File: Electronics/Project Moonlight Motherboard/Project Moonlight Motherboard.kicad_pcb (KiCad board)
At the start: 2 copper layers, 104.9 x 57.5 mm, 33 parts, among them M1 AO3400A, M2 AO3400A, M3 AO3400A, U1 Pico, U2 TMC2209_SILENTSTEPSTICK, U3 TMC2209_SILENTSTEPSTICK, U4 TMC2209_SILENTSTEPSTICK, U5 TMC2209_SILENTSTEPSTICK

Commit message: added headers for screen and rotary encoder, more tweaks
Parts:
- added ABL1: B2B-XH-A, B2B-XH-A:JST_B2B-XH-A, F.Cu at (193.1, 73.3)
- added R4: RC1206JR-134K7L, RC1206JR-134K7L:RESC3216X65, F.Cu at (202.8, 71.5)
- added R5: RC1206JR-134K7L, RC1206JR-134K7L:RESC3216X65, F.Cu at (202.8, 74.8)
- added R6: RC1206JR-134K7L, RC1206JR-134K7L:RESC3216X65, F.Cu at (201.5, 96.5)
- added REN1: PEC11H-4015F-S0016, Connector_PinHeader_2.54mm:PinHeader_1x04_P2.54mm_Vertical, F.Cu at (195.8, 108.1)
- added SCRN1: SSD1306, Connector_PinHeader_2.54mm:PinHeader_1x04_P2.54mm_Vertical, F.Cu at (195.8, 111.7)
- added ZES1: B2B-XH-A, B2B-XH-A:JST_B2B-XH-A, F.Cu at (184.2, 73.3)
- moved THM3 0.10 mm to (175.4, 73.3)
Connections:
- C5 pad 1: Net-(C5-Pad1) -> Net-(U1-GPIO13)
- C6 pad 1: Net-(C6-Pad1) -> Net-(U1-GPIO12)
- C7 pad 1: Net-(C7-Pad1) -> Net-(U1-GPIO11)
- R1 pad 2: Net-(C5-Pad1) -> Net-(U1-GPIO13)
- R2 pad 2: Net-(C6-Pad1) -> Net-(U1-GPIO12)
- R3 pad 2: Net-(C7-Pad1) -> Net-(U1-GPIO11)
- THM1 pad 2: Net-(C5-Pad1) -> Net-(U1-GPIO13)
- THM2 pad 2: Net-(C6-Pad1) -> Net-(U1-GPIO12)
- THM3 pad 2: Net-(C7-Pad1) -> Net-(U1-GPIO11)
- U1 pad 1: unconnected-(U1-GPIO0-Pad1) -> Net-(U1-GPIO0)
- U1 pad 14: unconnected-(U1-GPIO10-Pad14) -> Net-(REN1-W)
- U1 pad 15: unconnected-(U1-GPIO11-Pad15) -> Net-(U1-GPIO11)
- U1 pad 16: unconnected-(U1-GPIO12-Pad16) -> Net-(U1-GPIO12)
- U1 pad 17: unconnected-(U1-GPIO13-Pad17) -> Net-(U1-GPIO13)
- U1 pad 19: unconnected-(U1-GPIO14-Pad19) -> Net-(REN1-B)
- U1 pad 2: unconnected-(U1-GPIO1-Pad2) -> Net-(U1-GPIO1)
- U1 pad 20: unconnected-(U1-GPIO15-Pad20) -> Net-(REN1-A)
- U1 pad 31: unconnected-(U1-GPIO26_ADC0-Pad31) -> Net-(SCRN1-SDA)
- U1 pad 32: unconnected-(U1-GPIO27_ADC1-Pad32) -> Net-(SCRN1-SCL)
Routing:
- net +3V3: track 131.5 -> 205.0 mm, vias 4 -> 7
- net Net-(U1-GPIO12): track 0.00 -> 64.1 mm, vias 0 -> 3
- net Net-(REN1-A): track 0.00 -> 63.8 mm, vias 0 -> 6
- net Net-(REN1-B): track 0.00 -> 62.2 mm, vias 0 -> 6
- net Net-(REN1-W): track 0.00 -> 56.5 mm, vias 0 -> 5
- net Net-(C6-Pad1): track 49.6 -> 0.00 mm, vias 3 -> 0
- net Net-(U1-GPIO13): track 0.00 -> 45.0 mm, vias 0 -> 1
- net Net-(U1-GPIO11): track 0.00 -> 34.7 mm, vias 0 -> 1
- net Net-(C5-Pad1): track 33.5 -> 0.00 mm, vias 1 -> 0
- net Net-(U1-GPIO0): track 0.00 -> 32.0 mm, vias 0 -> 1
- net Net-(SCRN1-SDA): track 0.00 -> 29.7 mm, vias 0 -> 2
- net GNDREF: track 412.5 -> 439.4 mm, vias 4 -> 5
- net Net-(SCRN1-SCL): track 0.00 -> 24.7 mm, vias 0 -> 2
- net Net-(C7-Pad1): track 23.8 -> 0.00 mm, vias 1 -> 0
- net Net-(U1-GPIO1): track 0.00 -> 19.3 mm, vias 0 -> 1
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
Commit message: added a random resistor for UART - coming soon...
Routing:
- net Net-(U1-GPIO17): track 103.0 -> 105.4 mm
- net Net-(U1-GPIO9): track 79.9 -> 78.4 mm
- net Net-(U1-GPIO5): track 92.7 -> 91.8 mm
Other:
- outline, holes or cut-outs redrawn

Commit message: fixed schematic & added 3d model for MCU
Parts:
- removed ZES1: B2B-XH-A, B2B-XH-A:JST_B2B-XH-A
- added R7: RC0603FR-131KL, RC0603FR-131KL:0603, F.Cu at (51.2, 106.3)
- added Z_END1: B2B-XH-A, B2B-XH-A:JST_B2B-XH-A, F.Cu at (51.2, 87.0)
- U1: value Pico -> STM32F407IEHx; footprint MCU_RaspberryPi_and_Boards:RPi_Pico_SMD_TH -> Package_BGA:UFBGA-201_10x10mm_Layout15x15_P0.65mm
- moved C4 158.6 mm to (28.5, 111.3), turned to 0 degrees
- moved REN1 156.4 mm to (39.4, 107.6), turned to 0 degrees
- moved SCRN1 151.8 mm to (44.1, 107.6), turned to 0 degrees
- moved ABL1 151.6 mm to (41.6, 72.4), turned to 0 degrees
- moved C3 147.1 mm to (28.5, 99.1), turned to 0 degrees
- moved C2 136.8 mm to (28.5, 87.0), turned to 0 degrees
- moved R4 129.2 mm to (73.9, 80.4)
- moved R5 129.2 mm to (73.9, 83.7)
- moved R6 127.9 mm to (73.9, 87.0), turned to 0 degrees
- moved C1 127.9 mm to (28.5, 74.8), turned to 0 degrees
- moved C7 126.5 mm to (47.9, 110.6), turned to 0 degrees
- moved THM3 124.4 mm to (51.2, 79.7), turned to 0 degrees
- moved C6 122.8 mm to (47.9, 108.5), turned to 0 degrees
- moved PWR1 120.5 mm to (80.0, 95.0)
- moved C5 119.3 mm to (47.9, 106.3), turned to 0 degrees
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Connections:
- ABL1 pad 1: Net-(U1-GPIO1) -> ABL
- C5 pad 1: Net-(U1-GPIO13) -> T2
- C6 pad 1: Net-(U1-GPIO12) -> T1
- C7 pad 1: Net-(U1-GPIO11) -> T0
- M1 pad 1: Net-(U1-GPIO20) -> FAN1
- M2 pad 1: Net-(U1-GPIO21) -> FAN2
- M3 pad 1: Net-(U1-GPIO22) -> FAN3
- MOTOR_Y1 pad 1: Net-(U3-M1B) -> Net-(U4-M1B)
- MOTOR_Y1 pad 2: Net-(U3-M1A) -> Net-(U4-M1A)
- MOTOR_Y1 pad 3: Net-(U3-M2A) -> Net-(U4-M2A)
- MOTOR_Y1 pad 4: Net-(U3-M2B) -> Net-(U4-M2B)
- MOTOR_Z1 pad 1: Net-(U4-M1B) -> Net-(U3-M1B)
- MOTOR_Z1 pad 2: Net-(U4-M1A) -> Net-(U3-M1A)
- MOTOR_Z1 pad 3: Net-(U4-M2A) -> Net-(U3-M2A)
- MOTOR_Z1 pad 4: Net-(U4-M2B) -> Net-(U3-M2B)
- PWR1 pad 1: VCC -> Net-(F1-Pad1)
- Q1 pad 4: Net-(Q1-G) -> HOTEND
- Q2 pad 4: Net-(Q2-G) -> BED
- R1 pad 2: Net-(U1-GPIO13) -> T2
- R2 pad 2: Net-(U1-GPIO12) -> T1
- R3 pad 2: Net-(U1-GPIO11) -> T0
- R4 pad 1: Net-(U1-GPIO0) -> Z_END
- R5 pad 1: Net-(U1-GPIO1) -> ABL
- R6 pad 1: Net-(REN1-W) -> EN_BTN
- REN1 pad 1: Net-(REN1-A) -> EN_FOR
- REN1 pad 2: Net-(REN1-B) -> EN_REV
- REN1 pad 4: Net-(REN1-W) -> EN_BTN
- SCRN1 pad 3: Net-(SCRN1-SCL) -> SCRN_SCL
- SCRN1 pad 4: Net-(SCRN1-SDA) -> SCRN_SDA
- THM1 pad 2: Net-(U1-GPIO13) -> T2
- THM2 pad 2: Net-(U1-GPIO12) -> T1
- THM3 pad 2: Net-(U1-GPIO11) -> T0
- U2 pad 10: Net-(U1-GPIO2) -> STEP_M1
- U2 pad 12: unconnected-(U2-UART-Pad12) -> UART_RX
- U2 pad 16: Net-(U1-GPIO17) -> EN_M1
- U2 pad 18: unconnected-(U2-DIAG-Pad18) -> DIAG_M1
- U2 pad 9: Net-(U1-GPIO6) -> DIR_M1
- U3 pad 10: Net-(U1-GPIO3) -> STEP_M2
- U3 pad 12: unconnected-(U3-UART-Pad12) -> UART_RX
- U3 pad 16: Net-(U1-GPIO17) -> EN_M2
- U3 pad 18: unconnected-(U3-DIAG-Pad18) -> DIAG_M2
- U3 pad 9: Net-(U1-GPIO7) -> DIR_M2
- U4 pad 10: Net-(U1-GPIO4) -> STEP_M3
- U4 pad 12: unconnected-(U4-UART-Pad12) -> UART_RX
- U4 pad 16: Net-(U1-GPIO16) -> EN_M3
- U4 pad 18: unconnected-(U4-DIAG-Pad18) -> DIAG_M3
- U4 pad 9: Net-(U1-GPIO8) -> DIR_M3
- U5 pad 10: Net-(U1-GPIO5) -> STEP_M4
- U5 pad 12: unconnected-(U5-UART-Pad12) -> UART_RX
- U5 pad 16: Net-(U1-GPIO16) -> EN_M4
- U5 pad 18: unconnected-(U5-DIAG-Pad18) -> DIAG_M4
- U5 pad 9: Net-(U1-GPIO9) -> DIR_M4
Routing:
- net GNDREF: track 439.4 -> 0.00 mm, vias 5 -> 0
- net +3V3: track 205.0 -> 0.00 mm, vias 7 -> 0
- net VCC: track 201.0 -> 0.00 mm, vias 4 -> 0
- net Net-(U1-GPIO2): track 106.3 -> 0.00 mm
- net Net-(U1-GPIO17): track 105.4 -> 0.00 mm, vias 4 -> 0
- net Net-(U1-GPIO6): track 100.8 -> 0.00 mm
- net Net-(U1-GPIO16): track 97.0 -> 0.00 mm, vias 5 -> 0
- net Net-(U1-GPIO5): track 91.8 -> 0.00 mm, vias 1 -> 0
- net Net-(U1-GPIO9): track 78.4 -> 0.00 mm
- net Net-(U1-GPIO4): track 78.1 -> 0.00 mm, vias 1 -> 0
- net Net-(U1-GPIO3): track 72.4 -> 0.00 mm, vias 1 -> 0
- net Net-(U1-GPIO8): track 72.3 -> 0.00 mm, vias 2 -> 0
- net Net-(U1-GPIO12): track 64.1 -> 0.00 mm, vias 3 -> 0
- net Net-(REN1-A): track 63.8 -> 0.00 mm, vias 6 -> 0
- net Net-(REN1-B): track 62.2 -> 0.00 mm, vias 6 -> 0
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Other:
- board size 104.9 x 57.5 mm -> 105 x 50 mm

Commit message: slowly updating lmao
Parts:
- removed U1: STM32F407IEHx, Package_BGA:UFBGA-201_10x10mm_Layout15x15_P0.65mm
- added U6: STM32H563VITx, Package_QFP:LQFP-100_14x14mm_P0.5mm, F.Cu at (176.6, 95.7)
- moved SCRN1 157.4 mm to (200.6, 91.0)
- moved REN1 156.7 mm to (195.2, 91.0)
- moved PWR1 121.8 mm to (201.0, 108.6)
- moved U2 119.3 mm to (135.7, 117.9), turned to -90 degrees
- moved BED1 114.5 mm to (180.8, 127.7)
- moved M1 113.0 mm to (183.7, 75.5), turned to 90 degrees
- moved M2 109.8 mm to (179.1, 75.5), turned to 90 degrees
- moved M3 106.8 mm to (174.4, 75.5), turned to 90 degrees
- moved Q2 103.1 mm to (184.7, 114.1), turned to -90 degrees
- moved HOTEND1 100.8 mm to (169.9, 127.7)
- moved Q1 92.8 mm to (173.8, 114.1), turned to -90 degrees
- moved U3 87.2 mm to (113.1, 117.9), turned to -90 degrees
- moved MOTOR_X1 77.0 mm to (135.7, 106.0)
- moved MOTOR_Y1 72.8 mm to (135.7, 94.1), turned to 180 degrees
- moved U4 72.7 mm to (135.7, 82.1), turned to 90 degrees
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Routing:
- net GNDREF: track 0.00 -> 30.5 mm
- net HOTEND: track 0.00 -> 28.2 mm
- net BED: track 0.00 -> 19.7 mm
- net Net-(BED1-Pad01): track 0.00 -> 11.3 mm
- net Net-(HOTEND1-Pad01): track 0.00 -> 11.1 mm
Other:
- board size 105 x 50 mm -> 105 x 56 mm

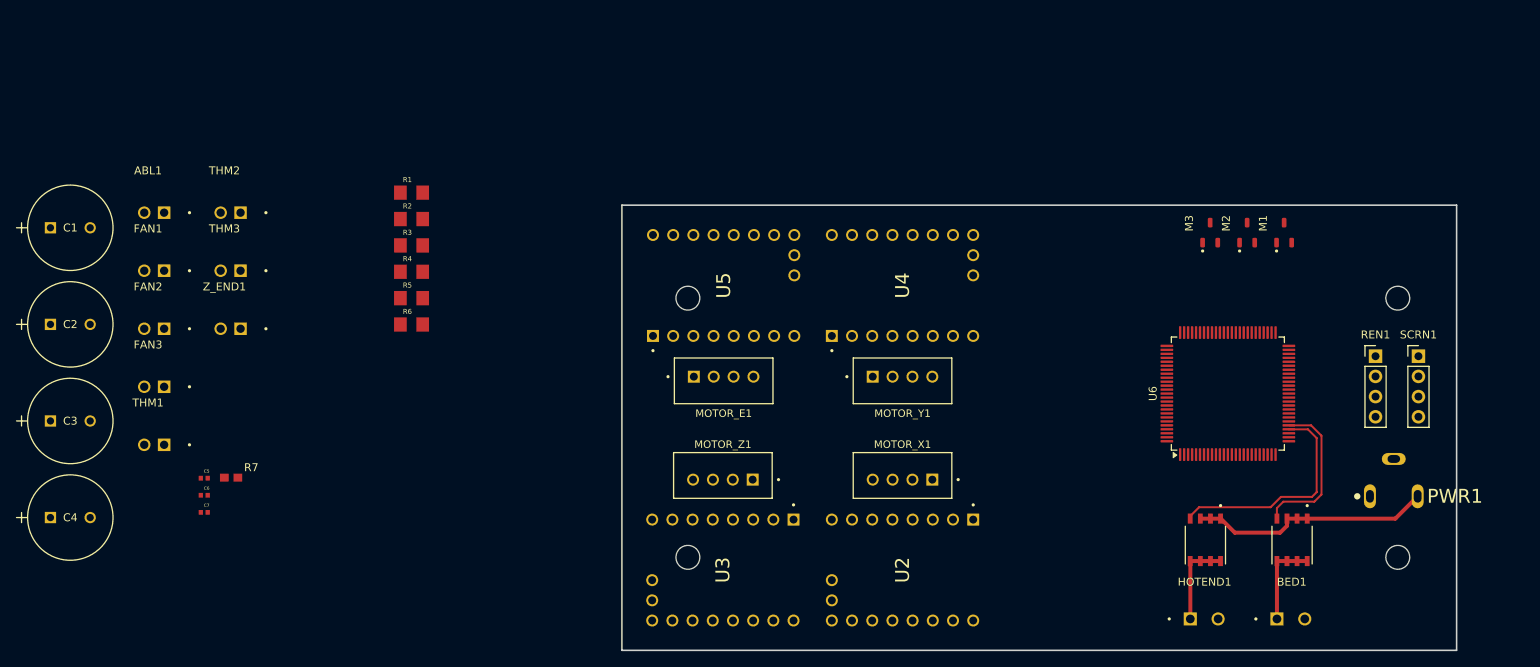
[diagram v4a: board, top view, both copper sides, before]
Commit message: added more parts and more routing done
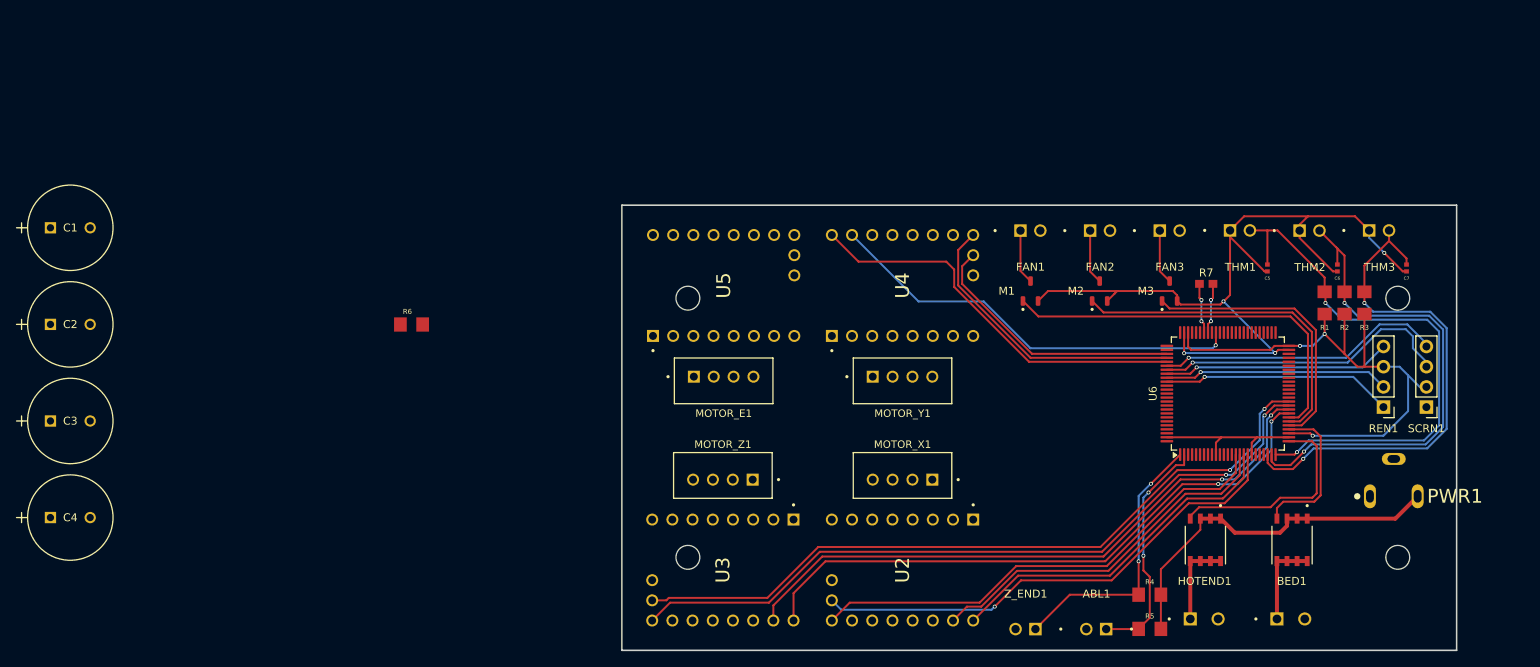
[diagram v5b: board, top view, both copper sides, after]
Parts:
- moved C7 154.3 mm to (199.1, 79.9), turned to -90 degrees
- moved C6 145.4 mm to (190.4, 79.9), turned to -90 degrees
- moved THM3 144.5 mm to (195.7, 75.7), turned to 180 degrees
- moved THM1 139.0 mm to (178.2, 75.7), turned to 180 degrees
- moved C5 136.3 mm to (181.6, 79.9), turned to -90 degrees
- moved THM2 135.8 mm to (186.9, 75.7), turned to 180 degrees
- moved ABL1 129.6 mm to (160.1, 124.8)
- moved FAN3 129.1 mm to (169.3, 75.7), turned to 180 degrees
- moved R7 125.1 mm to (173.9, 81.9), turned to 180 degrees
- moved R3 120.1 mm to (193.8, 84.3), turned to 90 degrees
- moved FAN2 119.5 mm to (160.6, 75.7), turned to 180 degrees
- moved R2 117.8 mm to (191.3, 84.3), turned to 90 degrees
- moved R1 115.7 mm to (188.8, 84.3), turned to 90 degrees
- moved FAN1 110.3 mm to (151.8, 75.7), turned to 180 degrees
- moved Z_END1 106.9 mm to (151.2, 124.8)
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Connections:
- U6 pad 1: unconnected-(U6-PE2-Pad1) -> Z_END
- U6 pad 2: unconnected-(U6-PE3-Pad2) -> ABL
- U6 pad 26: unconnected-(U6-PA3-Pad26) -> HOTEND
- U6 pad 29: HOTEND -> BED
- U6 pad 30: BED -> FAN3
- U6 pad 31: FAN1 -> FAN2
- U6 pad 32: FAN2 -> FAN1
- U6 pad 33: EN_M2 -> STEP_M2
- U6 pad 34: STEP_M2 -> EN_M2
- U6 pad 36: unconnected-(U6-PB1-Pad36) -> DIAG_M2
- U6 pad 64: DIAG_M2 -> unconnected-(U6-PC7-Pad64)
- U6 pad 65: EN_M3 -> EN_M4
- U6 pad 67: FAN3 -> unconnected-(U6-PA8-Pad67)
- U6 pad 68: unconnected-(U6-PA9-Pad68) -> UART_TX
- U6 pad 69: ABL -> UART_RX
- U6 pad 70: Z_END -> unconnected-(U6-PA11-Pad70)
- U6 pad 78: DIR_M3 -> DIAG_M3
- U6 pad 79: DIAG_M3 -> EN_M3
- U6 pad 80: EN_M4 -> DIR_M3
- U6 pad 83: EN_FOR -> EN_BTN
- U6 pad 85: EN_BTN -> EN_FOR
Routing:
- net GNDREF: track 30.5 -> 171.3 mm, vias 0 -> 4
- net EN_M2: track 0.00 -> 93.3 mm, vias 0 -> 2
- net DIAG_M2: track 0.00 -> 92.4 mm, vias 0 -> 2
- net STEP_M2: track 0.00 -> 79.0 mm, vias 0 -> 2
- net DIR_M2: track 0.00 -> 77.2 mm, vias 0 -> 2
- net +3V3: track 0.00 -> 70.5 mm, vias 0 -> 3
- net T2: track 0.00 -> 69.1 mm, vias 0 -> 2
- net T0: track 0.00 -> 64.6 mm, vias 0 -> 2
- net T1: track 0.00 -> 63.1 mm, vias 0 -> 2
- net DIAG_M1: track 0.00 -> 62.8 mm, vias 0 -> 1
- net EN_M1: track 0.00 -> 60.8 mm
- net STEP_M3: track 0.00 -> 53.4 mm, vias 0 -> 1
- net DIR_M3: track 0.00 -> 50.0 mm
- net FAN1: track 0.00 -> 49.8 mm
- net STEP_M1: track 0.00 -> 46.2 mm
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
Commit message: added capacitors and routed a bunch of things
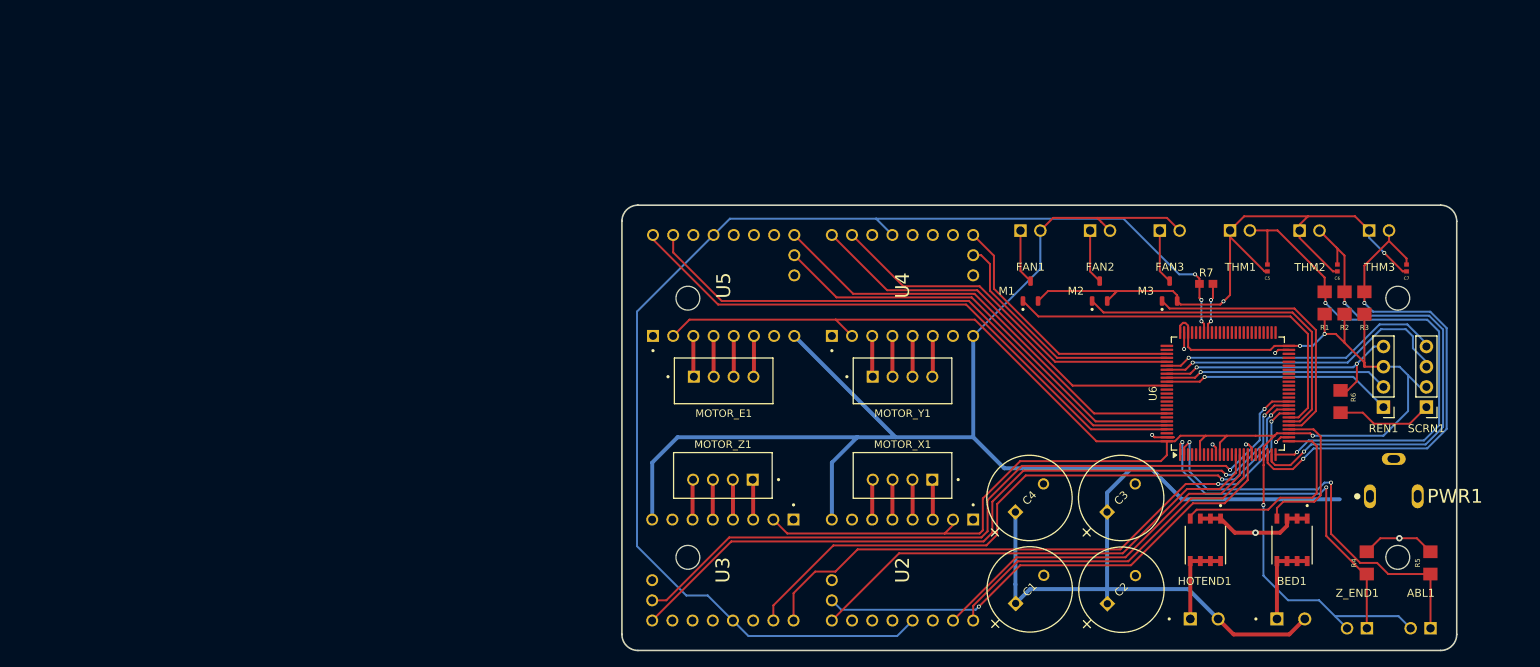
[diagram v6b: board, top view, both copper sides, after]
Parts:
- moved C2 137.5 mm to (161.5, 122.1), turned to 45 degrees
- moved C3 133.4 mm to (161.4, 110.6), turned to 45 degrees
- moved C1 130.3 mm to (149.9, 122.1), turned to 45 degrees
- moved C4 121.4 mm to (149.9, 110.6), turned to 45 degrees
- moved R6 117.3 mm to (190.8, 96.7), turned to -90 degrees
- moved Z_END1 41.7 mm to (192.9, 124.7)
- moved ABL1 40.8 mm to (200.9, 124.7)
- moved R5 36.3 mm to (202.1, 117.0), turned to 90 degrees
- moved R4 27.6 mm to (194.1, 117.0), turned to 90 degrees
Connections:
- U6 pad 33: STEP_M2 -> DIR_M2
- U6 pad 34: EN_M2 -> STEP_M2
- U6 pad 35: unconnected-(U6-PB0-Pad35) -> EN_M2
- U6 pad 63: DIR_M2 -> unconnected-(U6-PC6-Pad63)
- U6 pad 65: EN_M4 -> unconnected-(U6-PC8-Pad65)
- U6 pad 66: STEP_M3 -> unconnected-(U6-PC9-Pad66)
- U6 pad 7: STEP_M4 -> unconnected-(U6-PC13-Pad7)
- U6 pad 78: DIAG_M3 -> EN_M3
- U6 pad 79: EN_M3 -> DIAG_M3
- U6 pad 8: DIR_M4 -> unconnected-(U6-PC14-Pad8)
- U6 pad 80: DIR_M3 -> STEP_M3
- U6 pad 86: unconnected-(U6-PD5-Pad86) -> DIR_M3
- U6 pad 9: DIAG_M4 -> unconnected-(U6-PC15-Pad9)
- U6 pad 93: unconnected-(U6-PB7-Pad93) -> EN_M4
- U6 pad 95: unconnected-(U6-PB8-Pad95) -> DIAG_M4
- U6 pad 96: unconnected-(U6-PB9-Pad96) -> STEP_M4
- U6 pad 97: unconnected-(U6-PE0-Pad97) -> DIR_M4
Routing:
- net VCC: track 0.00 -> 250.9 mm
- net +3V3: track 70.5 -> 268.0 mm, vias 3 -> 4
- net UART_RX: track 6.36 -> 158.3 mm, vias 2 -> 3
- net DIR_M4: track 0.00 -> 75.1 mm
- net STEP_M4: track 0.00 -> 73.3 mm
- net EN_M4: track 0.00 -> 56.2 mm
- net DIAG_M4: track 0.00 -> 55.5 mm
- net GNDREF: track 171.3 -> 129.5 mm, vias 4 -> 10
- net ABL: track 29.7 -> 52.5 mm
- net Z_END: track 34.6 -> 44.9 mm
- net STEP_M3: track 53.4 -> 46.2 mm, vias 1 -> 0
- net Net-(U5-M2B): track 0.00 -> 5.15 mm
- net Net-(U5-M1B): track 0.00 -> 5.15 mm
- net Net-(U4-M2B): track 0.00 -> 5.15 mm
- net Net-(U4-M1B): track 0.00 -> 5.15 mm
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- added copper zone on In1.Cu, net GNDREF
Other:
- outline, holes or cut-outs redrawn
- copper layers 2 -> 4
